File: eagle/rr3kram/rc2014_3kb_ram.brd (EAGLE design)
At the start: 101.3 x 38.1 mm, 17 parts, among them IC7 74LS138N

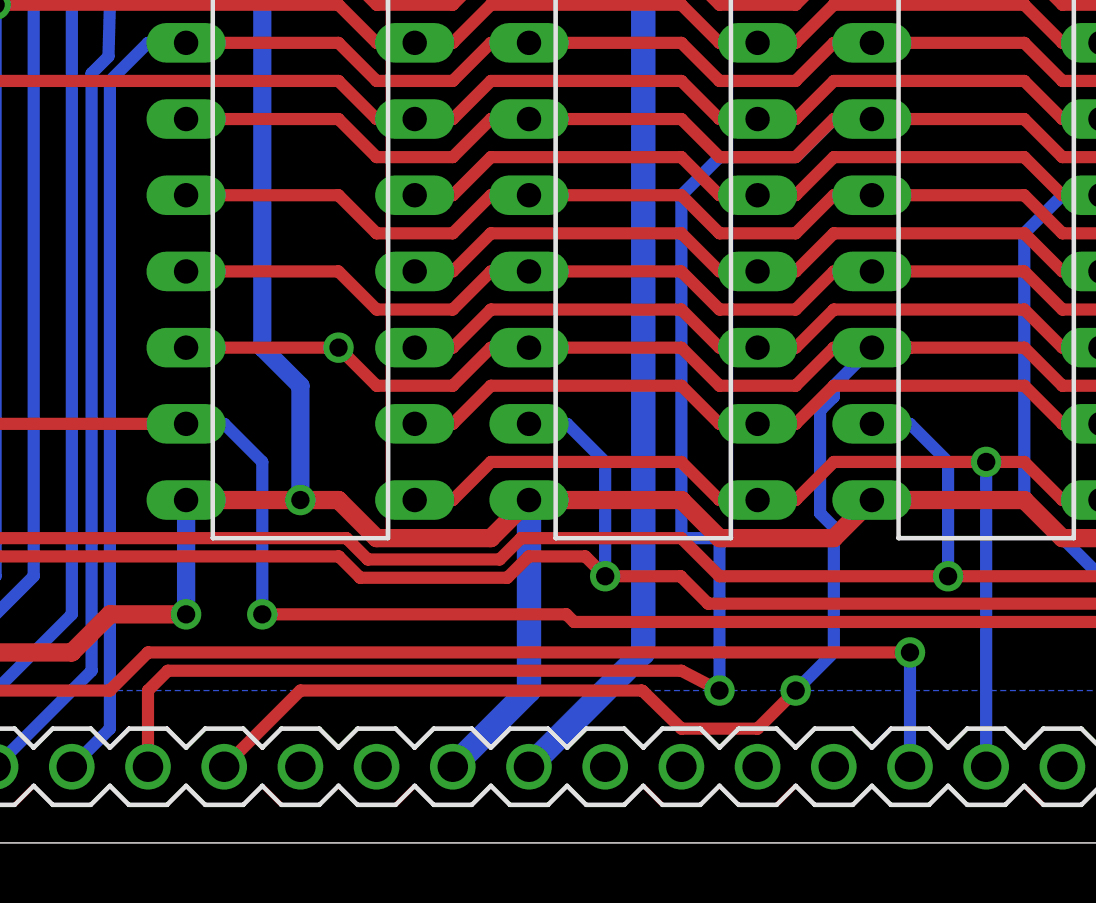
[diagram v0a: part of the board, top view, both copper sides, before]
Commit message: Fix missing A1, A0 lines
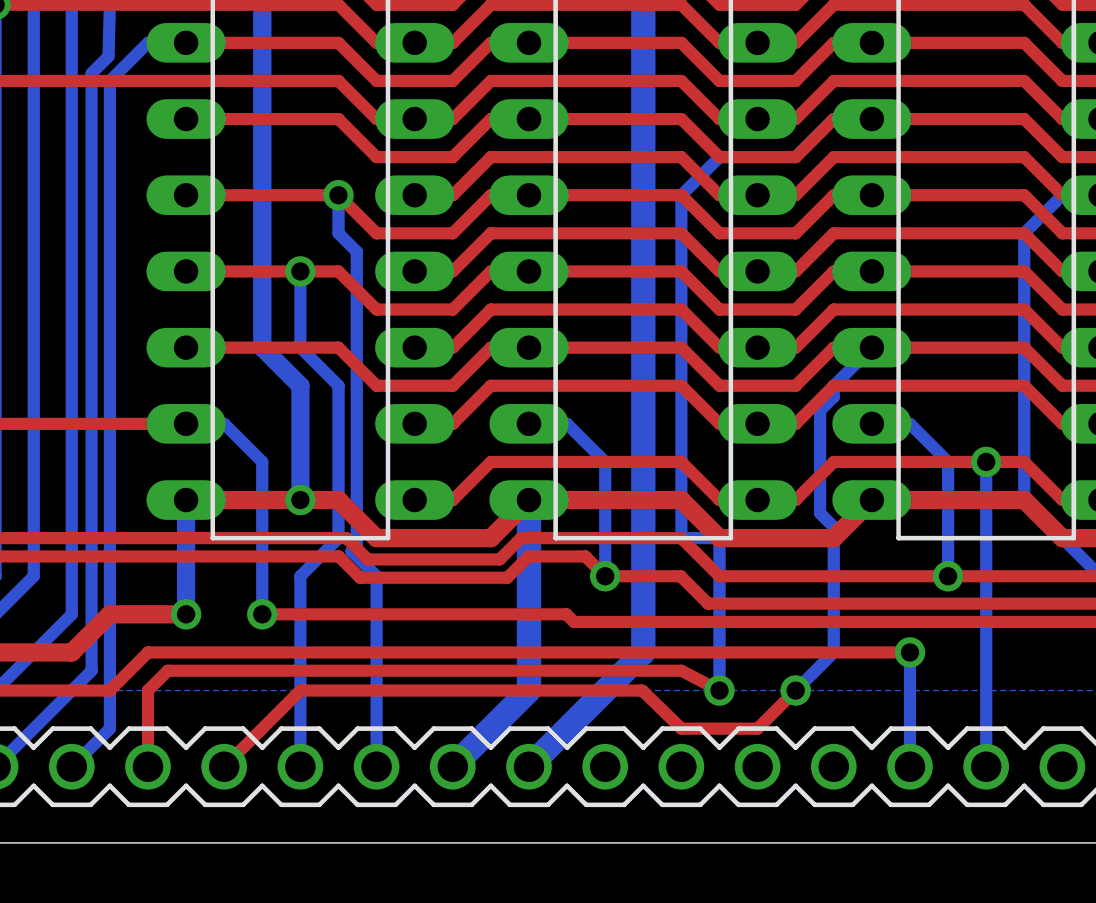
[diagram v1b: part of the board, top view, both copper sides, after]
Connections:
- net N$1 renamed /RD
- new net /INT: _PIN1.22
- new net /RST: _PIN1.20
- new net CLK: _PIN1.21
- net A0: now also _PIN1.16
- net A1: now also _PIN1.15
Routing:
- net A0: track 62.4 -> 82.1 mm, vias 0 -> 1
- net A1: track 62.4 -> 80.0 mm, vias 0 -> 1
- net A2: track 97.7 -> 96.4 mm, vias 2 -> 1
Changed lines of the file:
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@@
 <?xml version="1.0" encoding="utf-8"?>
 <!DOCTYPE eagle SYSTEM "eagle.dtd">
-<eagle version="8.1.0">
+<eagle version="8.1.1">
 <drawing>
 <settings>
@@
 <wire x1="87.63" y1="15.24" x2="88.9" y2="16.51" width="0.4064" layer="1"/>
 <wire x1="88.9" y1="16.51" x2="90.17" y2="16.51" width="0.4064" layer="1"/>
-<via x="38.1" y="16.51" extent="1-16" drill="0.6096"/>
 <via x="53.34" y="5.08" extent="1-16" drill="0.6096"/>
 <wire x1="55.88" y1="16.51" x2="54.61" y2="15.24" width="0.4064" layer="16"/>
@@
 <wire x1="50.8" y1="15.24" x2="53.34" y2="15.24" width="0.4064" layer="1"/>
 <wire x1="53.34" y1="15.24" x2="54.61" y2="16.51" width="0.4064" layer="1"/>
-<wire x1="54.61" y1="16.51" x2="57.15" y2="16.51" width="0.4064" layer="1"/>
+<wire x1="54.61" y1="16.51" x2="55.88" y2="16.51" width="0.4064" layer="1"/>
 </signal>
 <signal name="A1">
@@
 <contactref element="IC6" pad="6"/>
 <contactref element="IC3" pad="6"/>
-<wire x1="33.02" y1="19.05" x2="38.1" y2="19.05" width="0.4064" layer="1"/>
+<wire x1="33.02" y1="19.05" x2="36.83" y2="19.05" width="0.4064" layer="1"/>
+<wire x1="36.83" y1="19.05" x2="38.1" y2="19.05" width="0.4064" layer="1"/>
 <wire x1="38.1" y1="19.05" x2="39.37" y2="17.78" width="0.4064" layer="1"/>
 <wire x1="39.37" y1="17.78" x2="41.91" y2="17.78" width="0.4064" layer="1"/>
@@
 <wire x1="87.63" y1="17.78" x2="88.9" y2="19.05" width="0.4064" layer="1"/>
 <wire x1="88.9" y1="19.05" x2="90.17" y2="19.05" width="0.4064" layer="1"/>
+<contactref element="_PIN1" pad="15"/>
+<wire x1="36.83" y1="2.54" x2="36.83" y2="8.89" width="0.4064" layer="16"/>
+<wire x1="36.83" y1="8.89" x2="38.1" y2="10.16" width="0.4064" layer="16"/>
+<wire x1="38.1" y1="10.16" x2="38.1" y2="15.24" width="0.4064" layer="16"/>
+<wire x1="38.1" y1="15.24" x2="36.83" y2="16.51" width="0.4064" layer="16"/>
+<wire x1="36.83" y1="16.51" x2="36.83" y2="19.05" width="0.4064" layer="16"/>
+<via x="36.83" y="19.05" extent="1-16" drill="0.6096"/>
 </signal>
 <signal name="A0">
@@
 <wire x1="87.63" y1="20.32" x2="88.9" y2="21.59" width="0.4064" layer="1"/>
 <wire x1="88.9" y1="21.59" x2="90.17" y2="21.59" width="0.4064" layer="1"/>
-</signal>
-<signal name="/RST">
-</signal>
-<signal name="CLK">
-</signal>
-<signal name="/INT">
+<contactref element="_PIN1" pad="16"/>
+<wire x1="39.37" y1="2.54" x2="39.37" y2="8.89" width="0.4064" layer="16"/>
+<wire x1="39.37" y1="8.89" x2="38.531053125" y2="9.728946875" width="0.4064" layer="16"/>
+<wire x1="38.531053125" y1="9.728946875" x2="38.7096" y2="9.90749375" width="0.4064" layer="16"/>
+<wire x1="38.7096" y1="9.90749375" x2="38.7096" y2="19.7104" width="0.4064" layer="16"/>
+<wire x1="38.7096" y1="19.7104" x2="38.1" y2="20.32" width="0.4064" layer="16"/>
+<wire x1="38.1" y1="20.32" x2="38.1" y2="21.59" width="0.4064" layer="16"/>
+<via x="38.1" y="21.59" extent="1-16" drill="0.6096"/>
 </signal>
 <signal name="/MREQ">
@@
 <wire x1="20.32" y1="19.05" x2="19.05" y2="19.05" width="0.4064" layer="16"/>
 </signal>
-<signal name="N$1">
+<signal name="/RD">
 <contactref element="_PIN1" pad="25"/>
 </signal>
+<signal name="/RST">
+<contactref element="_PIN1" pad="20"/>
+</signal>
+<signal name="CLK">
+<contactref element="_PIN1" pad="21"/>
+</signal>
+<signal name="/INT">
+<contactref element="_PIN1" pad="22"/>
+</signal>
 </signals>
